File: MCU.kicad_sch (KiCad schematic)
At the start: 7 parts, among them U3 STM32G473QET6, U5 ADR4525

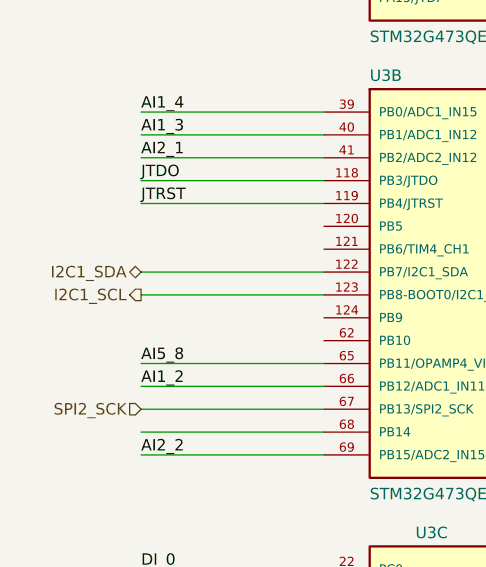
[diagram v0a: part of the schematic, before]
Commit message: Fleshed out digital IO
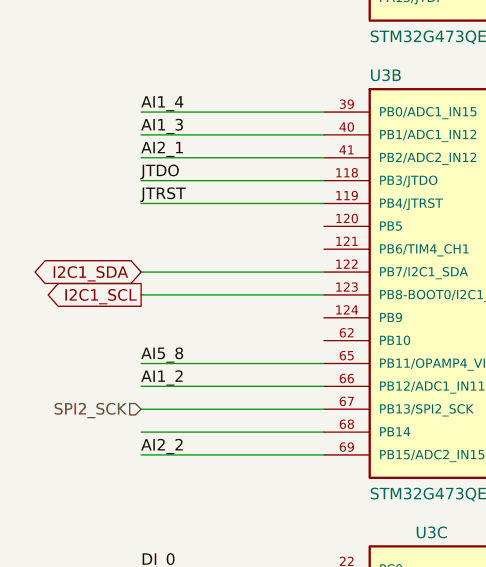
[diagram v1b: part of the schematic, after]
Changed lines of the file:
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@@
     (effects (font (size 1.27 1.27)) (justify left bottom))
+  )
+  (global_label "I2C1_SDA" (shape bidirectional) (at 38.1 93.98 180) (fields_autoplaced)
+    (effects (font (size 1.27 1.27)) (justify right))
+    (property "Intersheet References" "${INTERSHEET_REFS}" (id 0) (at 26.8574 93.9006 0)
+      (effects (font (size 1.27 1.27)) (justify right) hide)
+    )
+  )
+  (global_label "I2C1_SCL" (shape output) (at 38.1 96.52 180) (fields_autoplaced)
+    (effects (font (size 1.27 1.27)) (justify right))
+    (property "Intersheet References" "${INTERSHEET_REFS}" (id 0) (at 26.9179 96.4406 0)
+      (effects (font (size 1.27 1.27)) (justify right) hide)
+    )
   )
   (hierarchical_label "SPI4_SCK" (shape input) (at 114.3 106.68 180)
@@
   )
   (hierarchical_label "AI4_[6..1]" (shape input) (at 203.2 132.08 180)
-    (effects (font (size 1.27 1.27)) (justify right))
-  )
-  (hierarchical_label "I2C1_SCL" (shape output) (at 38.1 96.52 180)
     (effects (font (size 1.27 1.27)) (justify right))
   )
@@
     (effects (font (size 1.27 1.27)) (justify right))
   )
-  (hierarchical_label "I2C1_SDA" (shape bidirectional) (at 38.1 93.98 180)
-    (effects (font (size 1.27 1.27)) (justify right))
-  )

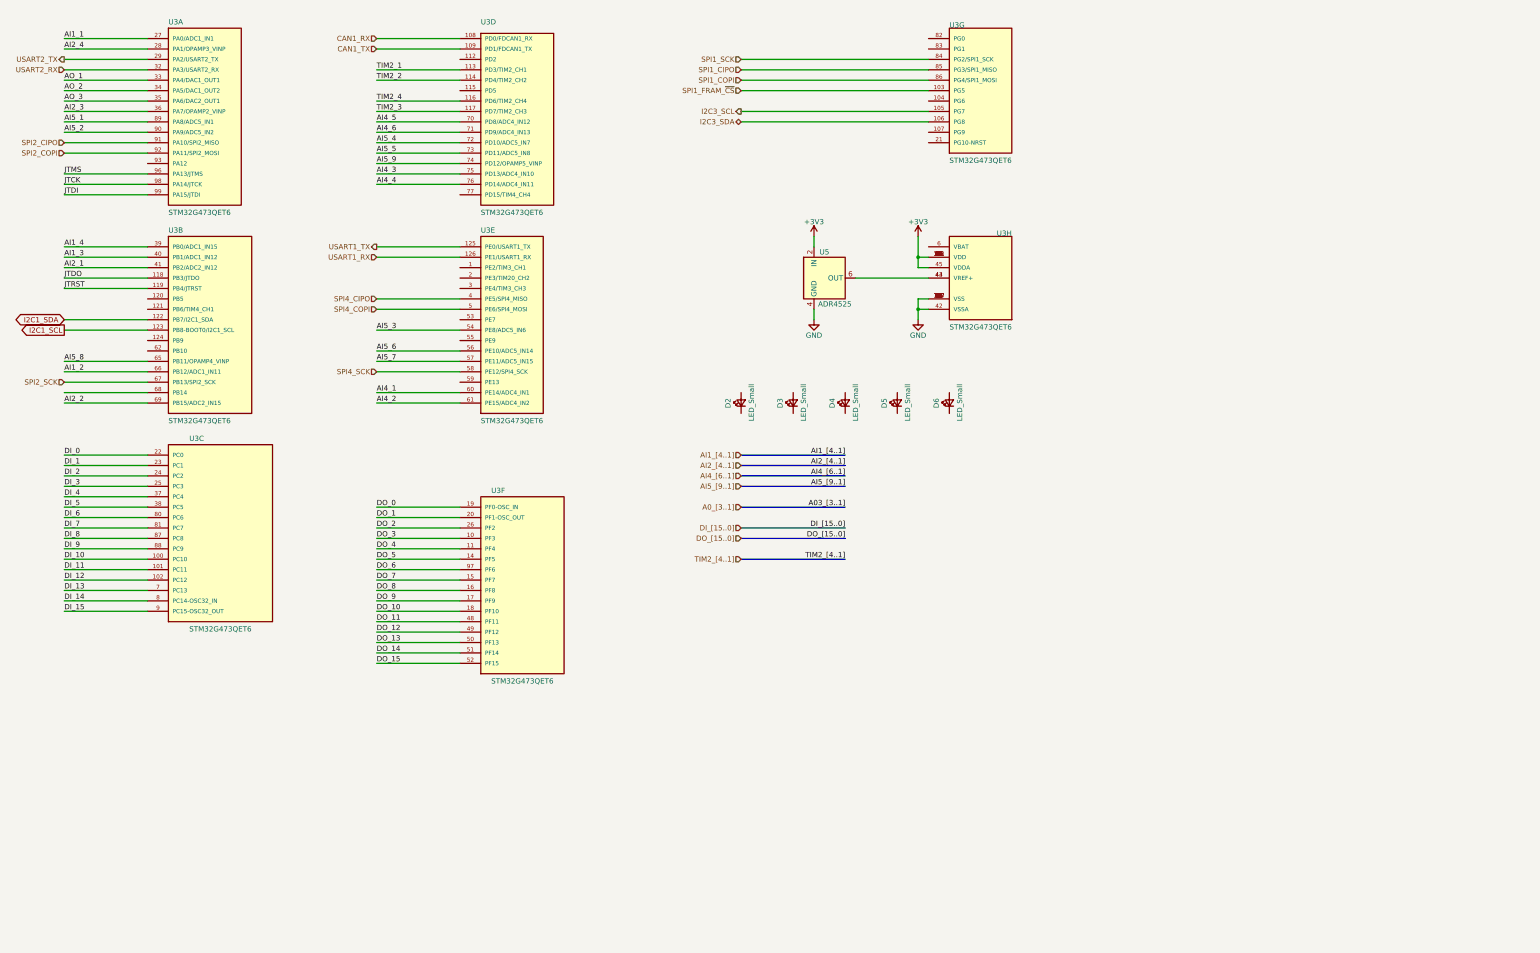
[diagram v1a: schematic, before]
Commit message: analog inputs, timer IO
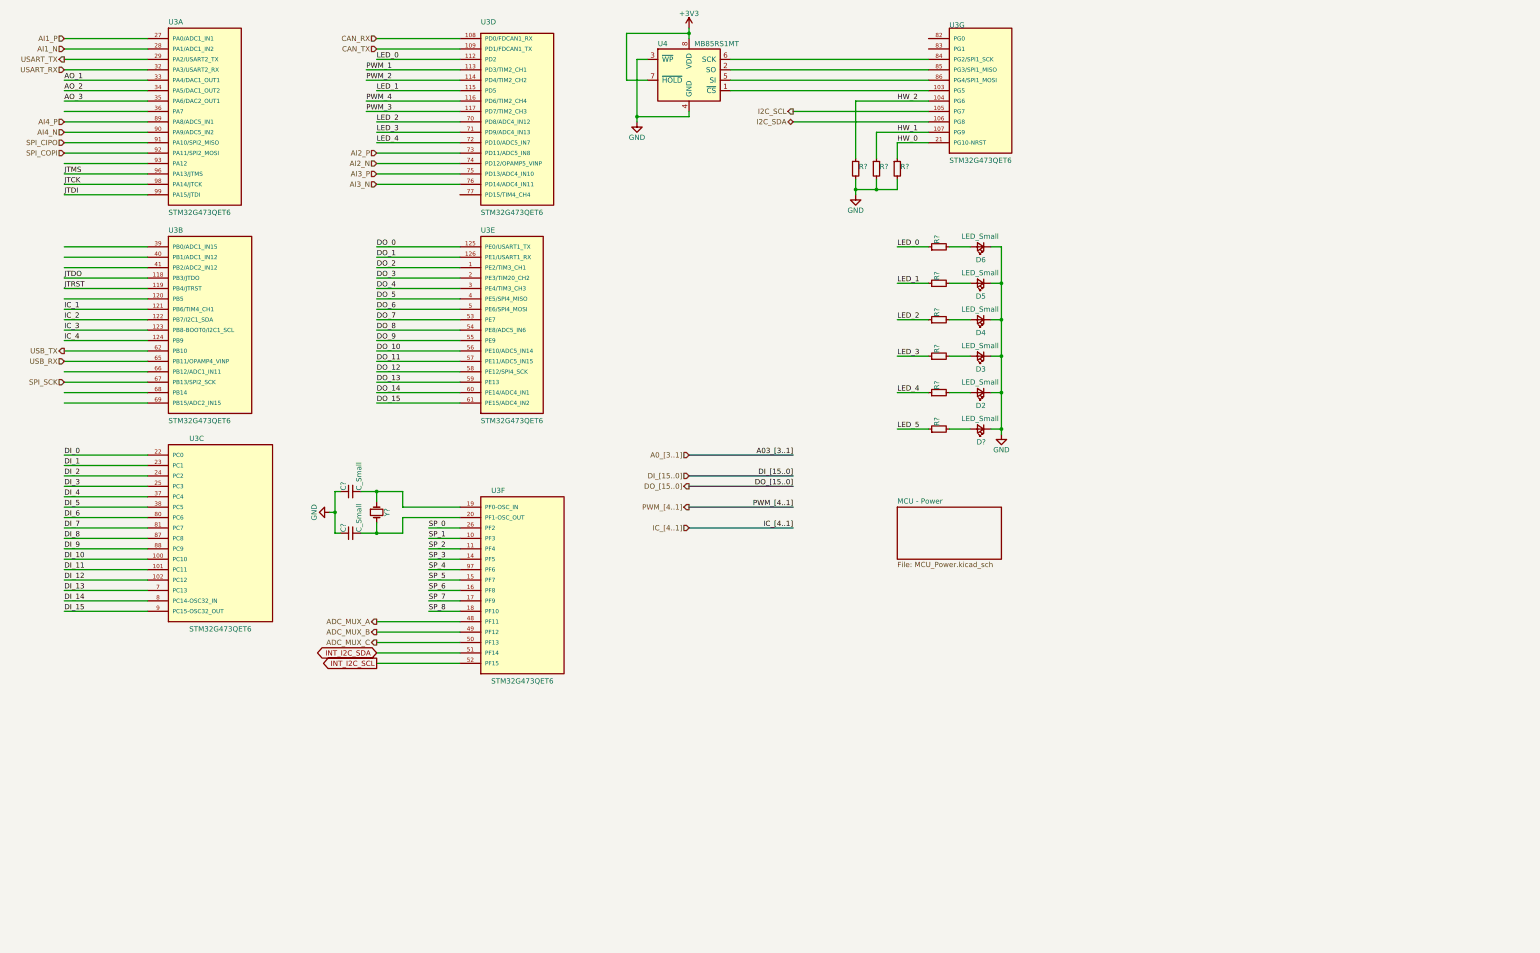
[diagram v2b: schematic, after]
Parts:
- removed unit 8 of U3
- removed U5: ADR4525, Package_SO:SOIC-8_3.9x4.9mm_P1.27mm, symbol Reference_Voltage:ADR4525
- added C? (x2): C_Small, symbol Device:C_Small
- added D?: LED_Small, symbol Device:LED_Small
- added R? (x6): R_Small, symbol Device:R_Small
- added R? (x3): R_0R_NNF, symbol Device:R_Small
- added U4: MB85RS1MT, Package_SO:SOIC-8_3.9x4.9mm_P1.27mm, symbol Memory_NVRAM:MB85RS1MT
- added Y?: Crystal_Small, symbol Device:Crystal_Small
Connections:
- net AI4_1 is gone; now on net DO_14: U3.60 (PE14/ADC4_IN1)
- net AI4_2 is gone; now on net DO_15: U3.61 (PE15/ADC4_IN2)
- net AI5_3 is gone; now on net DO_8: U3.54 (PE8/ADC5_IN6)
- net AI5_6 is gone; now on net DO_10: U3.56 (PE10/ADC5_IN14)
- net AI5_7 is gone; now on net DO_11: U3.57 (PE11/ADC5_IN15)
- net SPI4_CIPO is gone; now on net DO_5: U3.4 (PE5/SPI4_MISO)
- net SPI4_COPI is gone; now on net DO_6: U3.5 (PE6/SPI4_MOSI)
- net SPI4_SCK is gone; now on net DO_12: U3.58 (PE12/SPI4_SCK)
- net USART1_RX is gone; now on net DO_1: U3.126 (PE1/USART1_RX)
- net USART1_TX is gone; now on net DO_0: U3.125 (PE0/USART1_TX)
- net +3V3: now also U4.7 (~{HOLD}), U4.8 (VDD)
- net DO_0: no longer U3.19 (PF0-OSC_IN)
- net DO_1: no longer U3.20 (PF1-OSC_OUT)
- net DO_10: no longer U3.18 (PF10)
- net DO_11: no longer U3.48 (PF11)
- net DO_12: no longer U3.49 (PF12)
- net DO_13: now also U3.59 (PE13); no longer U3.50 (PF13)
- net DO_14: no longer U3.51 (PF14)
- net DO_15: no longer U3.52 (PF15)
- net DO_2: now also U3.1 (PE2/TIM3_CH1); no longer U3.26 (PF2)
- net DO_3: now also U3.2 (PE3/TIM20_CH2); no longer U3.10 (PF3)
- net DO_4: now also U3.3 (PE4/TIM3_CH3); no longer U3.11 (PF4)
- net DO_5: no longer U3.14 (PF5)
- net DO_6: no longer U3.97 (PF6)
- net DO_7: now also U3.53 (PE7); no longer U3.15 (PF7)
- net DO_8: no longer U3.16 (PF8)
- net DO_9: now also U3.55 (PE9); no longer U3.17 (PF9)
- net GND: now also D2.1 (K), D3.1 (K), D4.1 (K), D5.1 (K), D6.1 (K), C?.1, C?.1, D?.1 (K), R?.2, R?.2, R?.2, U4.3 (~{WP}), U4.4 (GND)
- net at D4.2 (A): now also R?.2
- net at D2.2 (A): now also R?.2
- net LED_0: now reaches U3.112 (PD2)
- net LED_0: now also R?.1
- net LED_1: now reaches U3.115 (PD5)
- net LED_1: now also R?.1
- net at D5.2 (A): now also R?.2
- net IC_1: now reaches U3.121 (PB6/TIM4_CH1)
- net IC_4: now reaches U3.124 (PB9)
- net USB_TX: now reaches U3.62 (PB10)
- net at D3.2 (A): now also R?.2
- net at D6.2 (A): now also R?.2
- net HW_2: now reaches U3.104 (PG6)
- net HW_2: now also R?.1
- net HW_1: now reaches U3.107 (PG9)
- net HW_1: now also R?.1
- net HW_0: now reaches U3.21 (PG10-NRST)
- net HW_0: now also R?.1
- net AI1_1 renamed AI1_P
- net AI1_2: no longer names the net of U3.66 (PB12/ADC1_IN11)
- net AI1_3: no longer names the net of U3.40 (PB1/ADC1_IN12)
- net AI1_4: no longer names the net of U3.39 (PB0/ADC1_IN15)
- net AI2_1: no longer names the net of U3.41 (PB2/ADC2_IN12)
- net AI2_2: no longer names the net of U3.69 (PB15/ADC2_IN15)
- net AI2_3: no longer names the net of U3.36 (PA7)
- net AI2_4 renamed AI1_N
- net AI4_3 renamed AI3_P
- net AI4_4 renamed AI3_N
- net AI4_5 renamed LED_2
- net LED_2: now also R?.1
- net AI4_6 renamed LED_3
- net LED_3: now also R?.1
- net AI5_1 renamed AI4_P
- net AI5_2 renamed AI4_N
- net AI5_4 renamed LED_4
- net LED_4: now also R?.1
- net AI5_5 renamed AI2_P
- net AI5_8 renamed USB_RX
- net AI5_9 renamed AI2_N
- net CAN1_RX renamed CAN_RX
- net CAN1_TX renamed CAN_TX
- net I2C1_SCL renamed IC_3
- net I2C1_SDA renamed IC_2
- net I2C3_SCL renamed I2C_SCL
- net I2C3_SDA renamed I2C_SDA
- net SPI1_CIPO: no longer names the net of U3.85 (PG3/SPI1_MISO)
- net SPI1_CIPO: now also U4.2 (SO)
- net SPI1_COPI: no longer names the net of U3.86 (PG4/SPI1_MOSI)
- net SPI1_COPI: now also U4.5 (SI)
- net SPI1_FRAM_~{CS}: no longer names the net of U3.103 (PG5)
- net SPI1_FRAM_~{CS}: now also U4.1 (~{CS})
- net SPI1_SCK: no longer names the net of U3.84 (PG2/SPI1_SCK)
- net SPI1_SCK: now also U4.6 (SCK)
- net SPI2_CIPO renamed SPI_CIPO
- net SPI2_COPI renamed SPI_COPI
- net SPI2_SCK renamed SPI_SCK
- net TIM2_1 renamed PWM_1
- net TIM2_2 renamed PWM_2
- net TIM2_3 renamed PWM_3
- net TIM2_4 renamed PWM_4
- net USART2_RX renamed USART_RX
- net USART2_TX renamed USART_TX
- new net: D?.2 (A), R?.2
- new net: C?.2, U3.19 (PF0-OSC_IN), Y?.1
- new net: C?.2, U3.20 (PF1-OSC_OUT), Y?.2
- new net ADC_MUX_A: U3.48 (PF11)
- new net ADC_MUX_B: U3.49 (PF12)
- new net ADC_MUX_C: U3.50 (PF13)
- new net INT_I2C_SCL: U3.52 (PF15)
- new net INT_I2C_SDA: U3.51 (PF14)
- new net LED_5: R?.1
- new net SP_0: U3.26 (PF2)
- new net SP_1: U3.10 (PF3)
- new net SP_2: U3.11 (PF4)
- new net SP_3: U3.14 (PF5)
- new net SP_4: U3.97 (PF6)
- new net SP_5: U3.15 (PF7)
- new net SP_6: U3.16 (PF8)
- new net SP_7: U3.17 (PF9)
- new net SP_8: U3.18 (PF10)
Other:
- added sheet MCU - Power (MCU_Power.kicad_sch)
- moved on the sheet: D2, D3, D4, D5, D6

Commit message: first draft schematic?
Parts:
- added D8, D9: LED_Small, LED_SMD:LED_0603_1608Metric, symbol Device:LED_Small
- added J6: Conn_ARM_JTAG_SWD_10, Connector_PinHeader_1.27mm:PinHeader_2x05_P1.27mm_Vertical_SMD, symbol Connector:Conn_ARM_JTAG_SWD_10
- added J7, J8: Conn_01x10, Connector_PinHeader_2.54mm:PinHeader_1x10_P2.54mm_Vertical, symbol Connector_Generic:Conn_01x10
- added R65, R66: R_Small, Resistor_SMD:R_0603_1608Metric, symbol Device:R_Small
- C49: renamed from C?; value C_Small -> C_0603_10%_10pF; footprint (none) -> Capacitor_SMD:C_0603_1608Metric; Capacitance (none) -> 10pf
- C50: renamed from C?; value C_Small -> C_0603_10%_10pF; footprint (none) -> Capacitor_SMD:C_0603_1608Metric; Capacitance (none) -> 10pF
- D2, D3, D4, D5, D6: footprint (none) -> LED_SMD:LED_0603_1608Metric
- D7: renamed from D?; footprint (none) -> LED_SMD:LED_0603_1608Metric
- R50, R57, R58, R59, R60, R61, R62, R63, R64: renamed from R?; footprint (none) -> Resistor_SMD:R_0603_1608Metric
- Y1: renamed from Y?; value Crystal_Small -> CRYSTAL_8MHZ_ABM3-8.000MHZ-D2Y-T; footprint (none) -> Crystal:Crystal_SMD_Abracon_ABM3-2Pin_5.0x3.2mm; Capacitance (none) -> 18pF; Frequency (none) -> 8MHz
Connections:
- net +3V3: now also J6.1 (VTref), J7.1 (Pin_1), J8.1 (Pin_1)
- net GND: now also D8.1 (K), D9.1 (K), J6.3 (GND), J6.5 (GND), J6.9 (GNDDetect), J7.10 (Pin_10), J7.2 (Pin_2), J8.10 (Pin_10), J8.2 (Pin_2)
- net JTCK: now also J6.4 (SWDCLK/TCK)
- net JTDI: now also J6.8 (NC/TDI)
- net JTDO: now also J6.6 (SWO/TDO)
- net JTMS: now also J6.2 (SWDIO/TMS)
- net JTRST: now also J6.10 (~{RESET})
- net LED_5: now also U3.77 (PD15/TIM4_CH4)
- net SP_0: now also J7.3 (Pin_3)
- net SP_1: now also J7.4 (Pin_4)
- net SP_2: now also J7.5 (Pin_5)
- net SP_3: now also J7.6 (Pin_6)
- net SP_4: now also J7.7 (Pin_7)
- net SP_5: now also J7.8 (Pin_8)
- net SP_6: now also J7.9 (Pin_9)
- net SP_7: now also J8.9 (Pin_9)
- net SP_8: now also J8.3 (Pin_3)
- net LED_6: now reaches U3.36 (PA7)
- net LED_6: now also R65.1
- net LED_7: now reaches U3.93 (PA12)
- net LED_7: now also R66.1
- net SP_10: now reaches U3.120 (PB5)
- net SP_10: now also J8.5 (Pin_5)
- net PWM_7: now reaches U3.39 (PB0/ADC1_IN15)
- net PWM_8: now reaches U3.40 (PB1/ADC1_IN12)
- net SP_9: now reaches U3.41 (PB2/ADC2_IN12)
- net SP_9: now also J8.4 (Pin_4)
- net SP_11: now reaches U3.66 (PB12/ADC1_IN11)
- net SP_11: now also J8.6 (Pin_6)
- net PWM_5: now reaches U3.68 (PB14)
- net PWM_6: now reaches U3.69 (PB15/ADC2_IN15)
- net SP_12: now reaches U3.82 (PG0)
- net SP_12: now also J8.7 (Pin_7)
- net SP_13: now reaches U3.83 (PG1)
- net SP_13: now also J8.8 (Pin_8)
- new net: D8.2 (A), R65.2
- new net: D9.2 (A), R66.2
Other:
- moved on the sheet: C49, C50, D2, D3, D4, D5, D6, D7, R59, R60, R61, R62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
